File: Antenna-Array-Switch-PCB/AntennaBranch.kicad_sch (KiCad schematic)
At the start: 15 parts, among them J1 Conn_Coaxial, U1 PGA-103, U2 TPS22917DBV

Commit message: PCB: Assign footprints where sensible
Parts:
- added D4: LED, LED_SMD:LED_0603_1608Metric_Pad1.05x0.95mm_HandSolder, symbol Device:LED
- added R10: 10k, Resistor_SMD:R_0603_1608Metric_Pad0.98x0.95mm_HandSolder, symbol Device:R
- C1: renamed from C; footprint (none) -> Capacitor_SMD:C_0603_1608Metric_Pad1.08x0.95mm_HandSolder
- C2, C5, C6, C7, C8, C9: footprint (none) -> Capacitor_SMD:C_0603_1608Metric_Pad1.08x0.95mm_HandSolder
- L1: renamed from L; footprint (none) -> Inductor_SMD:L_0603_1608Metric_Pad1.05x0.95mm_HandSolder; LCSC (none) -> C21202145; Part (none) -> 9-1624112-0
- R1, R2: renamed from R; footprint (none) -> Resistor_SMD:R_0603_1608Metric_Pad0.98x0.95mm_HandSolder
- R3: footprint (none) -> Resistor_SMD:R_0603_1608Metric_Pad0.98x0.95mm_HandSolder
- renumbered D to D1
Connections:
- net GNDA: now also D4.1 (K)
- net LNA_ENABLE: now also R10.1
- new net: D4.2 (A), R10.2
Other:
- moved on the sheet: C2, L1

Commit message: PCB: Add MCU, switch
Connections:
- net GNDA: no longer D4.1 (K)
- new net GNDD: D4.1 (K)
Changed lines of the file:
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@@
 	(wire
 		(pts
-			(xy 81.28 46.99) (xy 88.9 46.99)
+			(xy 85.09 46.99) (xy 88.9 46.99)
 		)
 		(stroke
@@
 	(hierarchical_label "LNA_ENABLE"
 		(shape input)
-		(at 81.28 46.99 180)
+		(at 85.09 46.99 180)
 		(effects
 			(font
@@
 			)
 			(justify left)
-		)
-	)
-	(symbol
-		(lib_id "power:GNDA")
-		(at 88.9 71.12 0)
-		(unit 1)
-		(body_style 1)
-		(exclude_from_sim no)
-		(in_bom yes)
-		(on_board yes)
-		(in_pos_files yes)
-		(dnp no)
-		(property "Reference" "#PWR027"
-			(at 88.9 77.47 0)
-			(hide yes)
-			(show_name no)
-			(do_not_autoplace no)
-			(effects
-				(font
-					(size 1.27 1.27)
-				)
-			)
-		)
-		(property "Value" "GNDA"
-			(at 88.9 74.93 0)
-			(show_name no)
-			(do_not_autoplace no)
-			(effects
-				(font
-					(size 1.27 1.27)
-				)
-			)
-		)
-		(property "Footprint" "Package_TO_SOT_SMD:SOT-23-6"
-			(at 88.9 71.12 0)
-			(hide yes)
-			(show_name no)
-			(do_not_autoplace no)
-			(effects
-				(font
-					(size 1.27 1.27)
-				)
-			)
-		)
-		(property "Datasheet" ""
-			(at 88.9 71.12 0)
-			(hide yes)
-			(show_name no)
-			(do_not_autoplace no)
-			(effects
-				(font
-					(size 1.27 1.27)
-				)
-			)
-		)
-		(property "Description" "Power symbol creates a global label with name \"GNDA\" , analog ground"
-			(at 88.9 71.12 0)
-			(hide yes)
-			(show_name no)
-			(do_not_autoplace no)
-			(effects
-				(font
-					(size 1.27 1.27)
-				)
-			)
-		)
-		(pin "1"
-		)
-		(instances
-			(project "Antenna-Array-Switch-PCB"
-				(path "/53a2d682-f221-4d2b-9002-0fe959bb1f68/872b3e63-a37e-49b3-8d67-29eb300db3b2"
-					(reference "#PWR029")
-					(unit 1)
-				)
-				(path "/53a2d682-f221-4d2b-9002-0fe959bb1f68/a3b68118-00d6-43dd-924e-52a6fbdf55d7"
-					(reference "#PWR027")
-					(unit 1)
-				)
-				(path "/53a2d682-f221-4d2b-9002-0fe959bb1f68/b56fce60-6d4e-44ca-8002-6e4783aa0201"
-					(reference "#PWR028")
-					(unit 1)
-				)
-			)
 		)
 	)
@@
 					(unit 1)
 				)
+			)
+		)
+	)
+	(symbol
+		(lib_id "power:GNDD")
+		(at 88.9 71.12 0)
+		(unit 1)
+		(body_style 1)
+		(exclude_from_sim no)
+		(in_bom yes)
+		(on_board yes)
+		(in_pos_files yes)
+		(dnp no)
+		(fields_autoplaced yes)
+		(property "Reference" "#PWR027"
+			(at 88.9 77.47 0)
+			(hide yes)
+			(show_name no)
+			(do_not_autoplace no)
+			(effects
+				(font
+					(size 1.27 1.27)
+				)
+			)
+		)
+		(property "Value" "GNDD"
+			(at 88.9 74.93 0)
+			(show_name no)
+			(do_not_autoplace no)
+			(effects
+				(font
+					(size 1.27 1.27)
+				)
+			)
+		)
+		(property "Footprint" ""
+			(at 88.9 71.12 0)
+			(hide yes)
+			(show_name no)
+			(do_not_autoplace no)
+			(effects
+				(font
+					(size 1.27 1.27)
+				)
+			)
+		)
+		(property "Datasheet" ""
+			(at 88.9 71.12 0)
+			(hide yes)
+			(show_name no)
+			(do_not_autoplace no)
+			(effects
+				(font
+					(size 1.27 1.27)
+				)
+			)
+		)
+		(property "Description" "Power symbol creates a global label with name \"GNDD\" , digital ground"
+			(at 88.9 71.12 0)
+			(hide yes)
+			(show_name no)
+			(do_not_autoplace no)
+			(effects
+				(font
+					(size 1.27 1.27)
+				)
+			)
+		)
+		(pin "1"
+		)
+		(instances
+			(project "Antenna-Array-Switch-PCB"
+				(path "/53a2d682-f221-4d2b-9002-0fe959bb1f68/872b3e63-a37e-49b3-8d67-29eb300db3b2"
+					(reference "#PWR029")
+					(unit 1)
+				)
+				(path "/53a2d682-f221-4d2b-9002-0fe959bb1f68/a3b68118-00d6-43dd-924e-52a6fbdf55d7"
+					(reference "#PWR027")
+					(unit 1)
+				)
+				(path "/53a2d682-f221-4d2b-9002-0fe959bb1f68/b56fce60-6d4e-44ca-8002-6e4783aa0201"
+					(reference "#PWR028")
+					(unit 1)
+				)

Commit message: PCB: Layout an LNA segment
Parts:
- J1: footprint Filter:Filter_1411-5_1.4x1.1mm -> Connector_Coaxial:SMA_Amphenol_901-144_Vertical
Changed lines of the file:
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@@
 			)
 		)
-		(property "Footprint" "Filter:Filter_1411-5_1.4x1.1mm"
+		(property "Footprint" "Connector_Coaxial:SMA_Amphenol_901-144_Vertical"
 			(at 54.61 115.57 0)
 			(hide yes)

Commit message: PCB, Docs: Layout, stackup, shielding
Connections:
- net GNDD is gone; now on net GNDA: D4.1 (K)

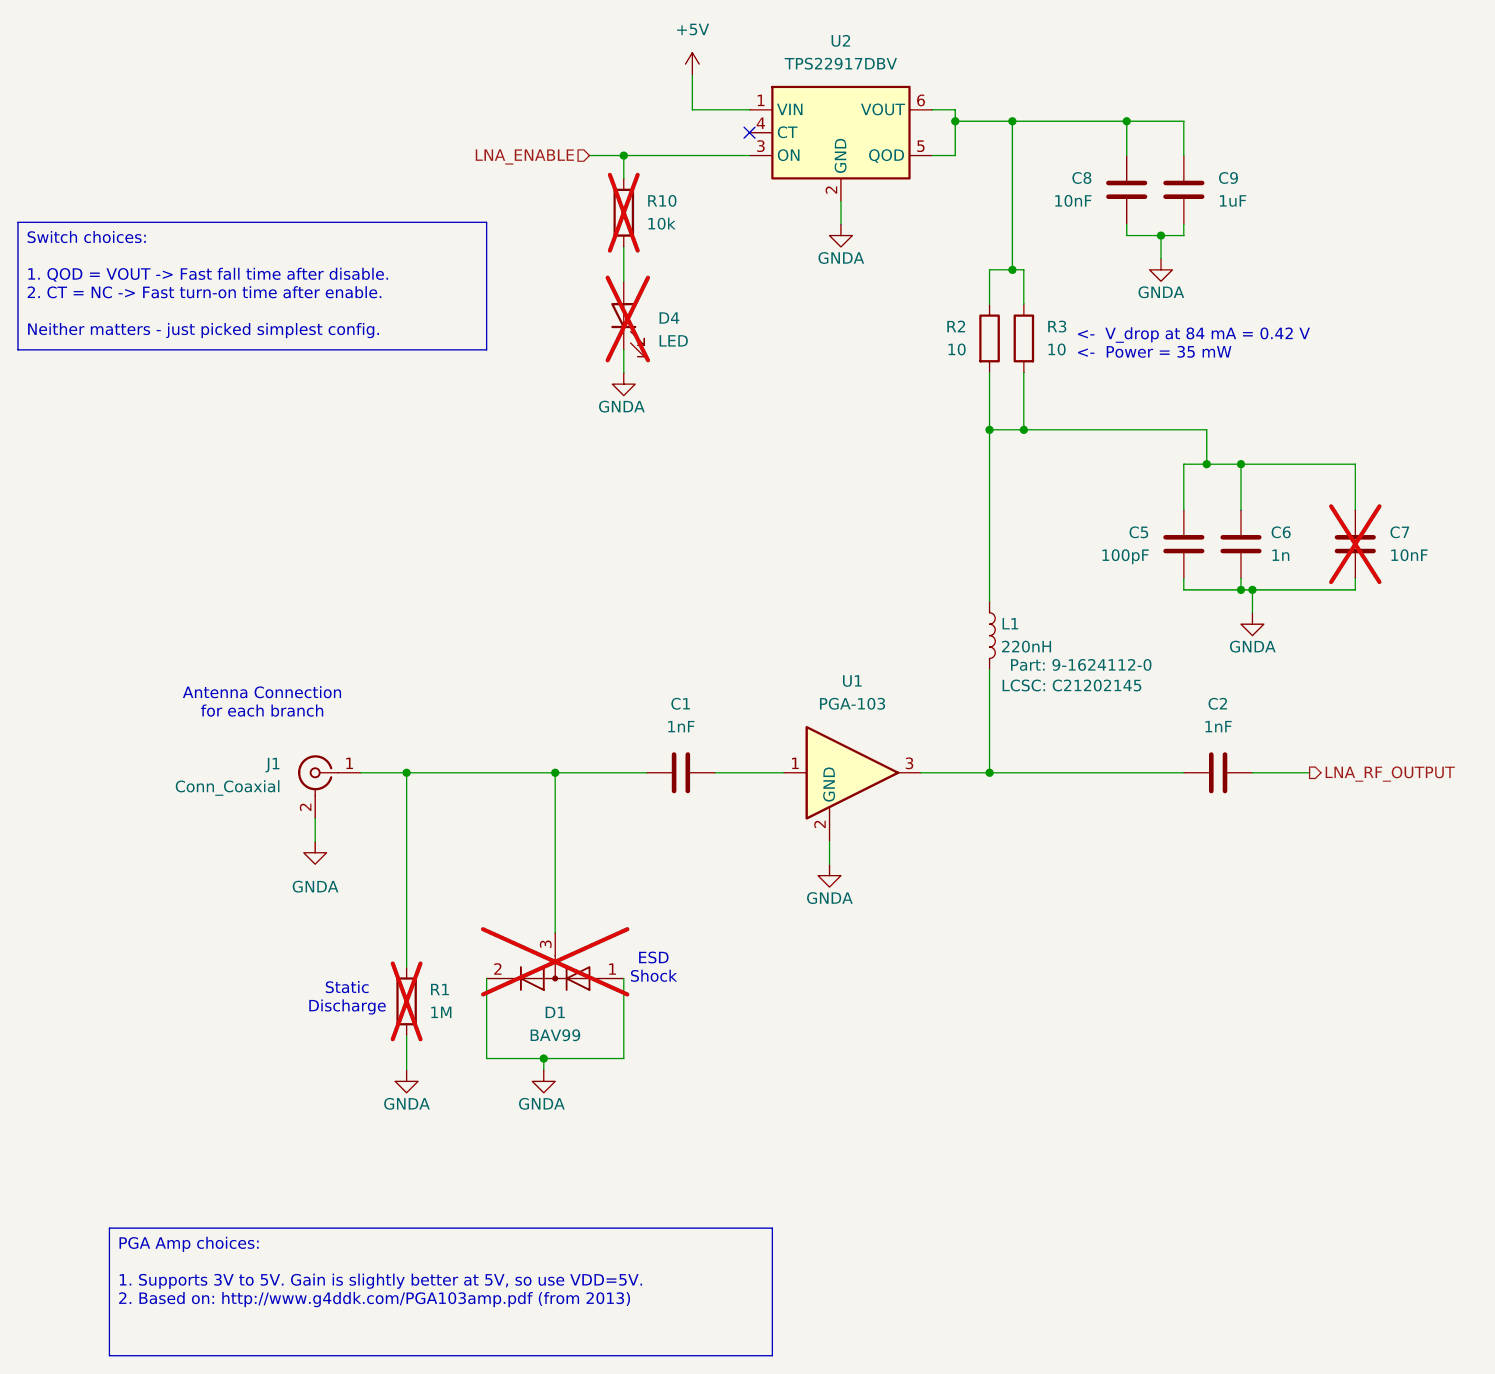
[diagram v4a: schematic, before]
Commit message: PCB: Replicate layouts to all LNA chains
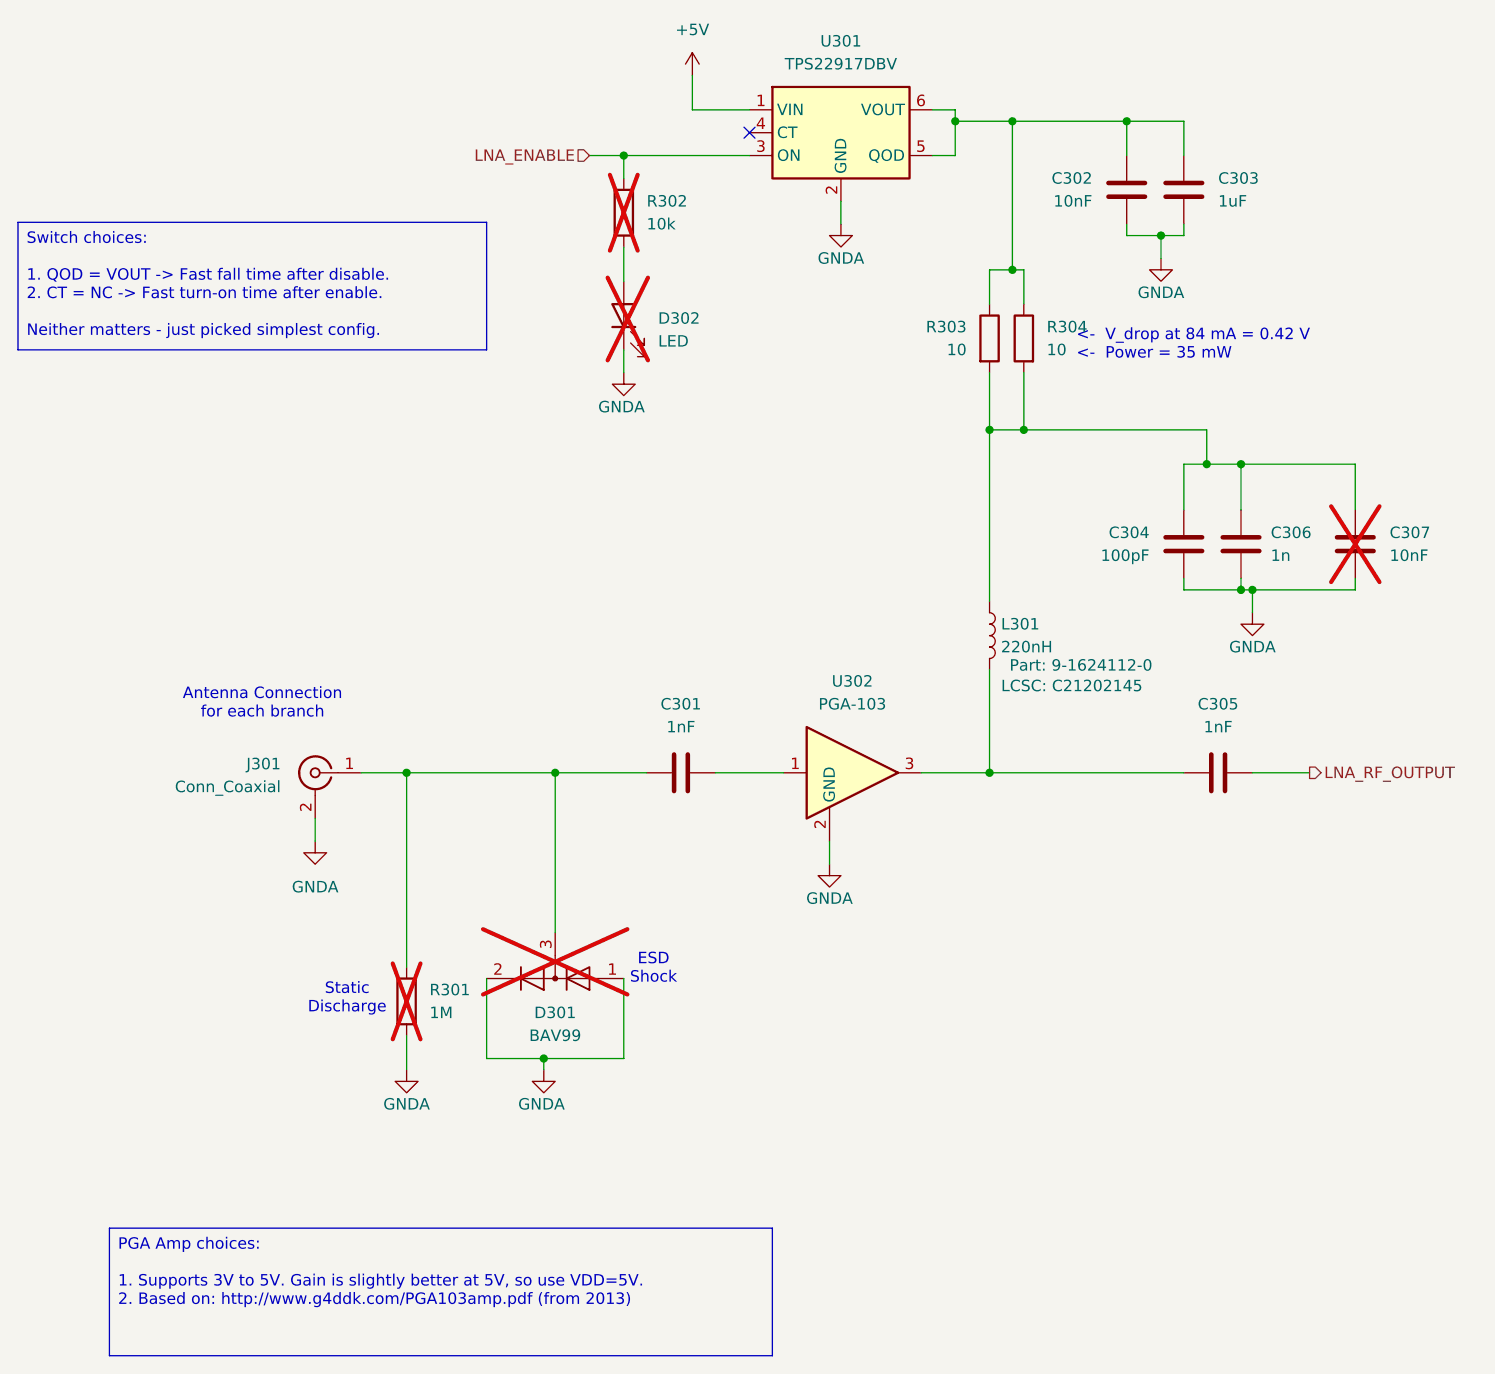
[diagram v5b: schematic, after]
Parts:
- renumbered C1 to C301, C8 to C302, C9 to C303, C5 to C304, C2 to C305, C6 to C306, C7 to C307, D1 to D301, D4 to D302, J1 to J301, L1 to L301, R1 to R301, R10 to R302, R2 to R303, R3 to R304, U2 to U301, U1 to U302

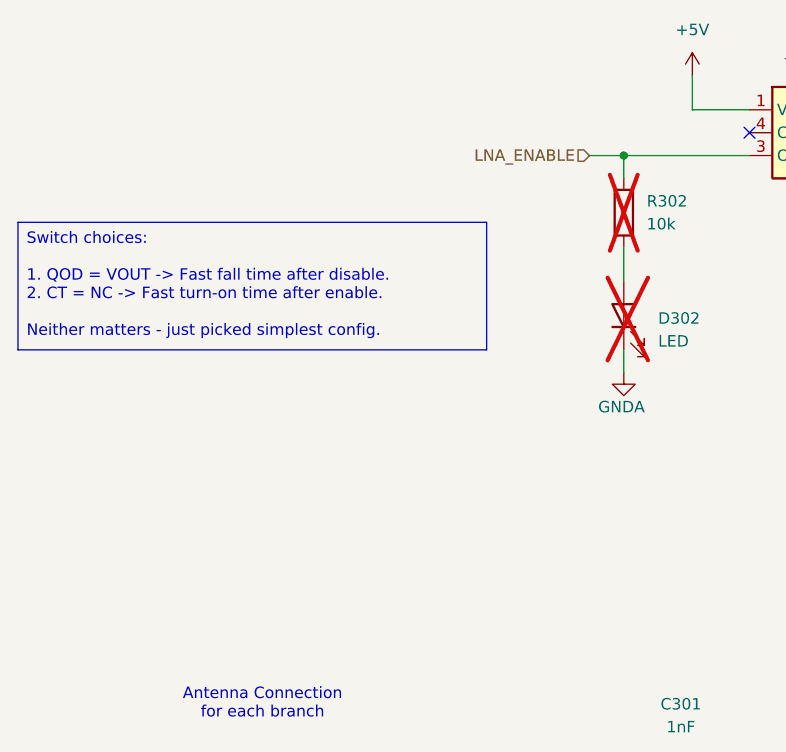
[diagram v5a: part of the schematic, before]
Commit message: PCB Sch: Add filters at control lines
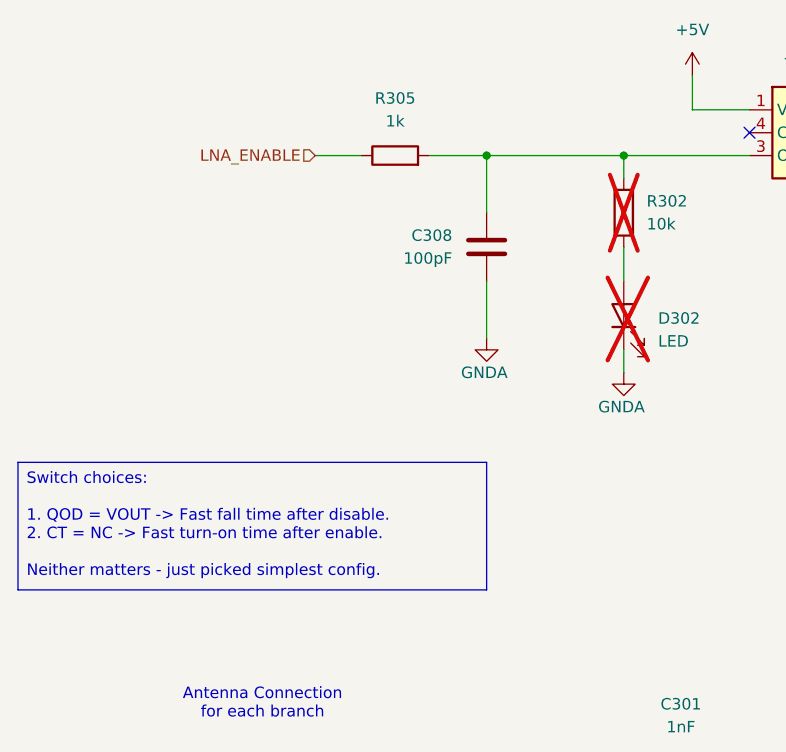
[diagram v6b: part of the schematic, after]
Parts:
- added C308: 100pF, Capacitor_SMD:C_0603_1608Metric_Pad1.08x0.95mm_HandSolder, symbol Device:C
- added R305: 1k, Resistor_SMD:R_0603_1608Metric_Pad0.98x0.95mm_HandSolder, symbol Device:R
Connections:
- net GNDA: now also C308.1
- net LNA_ENABLE: now also R305.1; no longer R302.1, U301.3 (ON)
- new net: C308.2, R302.1, R305.2, U301.3 (ON)

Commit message: PCB: Update LCSC assignments for ordering
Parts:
- removed D301: BAV99, Package_TO_SOT_SMD:SOT-23, symbol Diode:BAV99
- added D303: ESD131-B1-W0201, Diode_SMD:Infineon_SG-WLL-2-3_0.58x0.28_P0.36mm, symbol Diode:ESD131-B1-W0201
- C301, C305: LCSC (none) -> C77026
- C304: LCSC (none) -> C14858
- C306: value 1n -> 1nF; LCSC (none) -> C77026
- C307, D302, R301, R302: now fitted
- L301: footprint Inductor_SMD:L_0603_1608Metric_Pad1.05x0.95mm_HandSolder -> Inductor_SMD:L_0805_2012Metric_Pad1.05x1.20mm_HandSolder; LCSC C21202145 -> C337958; Part 9-1624112-0 -> LQW2BASR22J00L
- U302: value PGA-103 -> PGA-103+; LCSC (none) -> C3008207
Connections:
- net GNDA: now also D303.1 (A1)
- net at C301.1, J301.1 (In), R301.1: now also D303.2 (A2)
